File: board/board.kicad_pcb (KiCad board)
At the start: 4 copper layers, 45 x 157 mm, 47 parts, among them J1 020_1000BASE-T_with_CT, J2 020_1000BASE-T_with_CT, J3 020_1000BASE-T_with_CT, J4 020_1000BASE-T_with_CT, J5 020_1000BASE-T_with_CT, J6 011_GPIO, U1 RTL8367S-CG, Y1 25MhZ

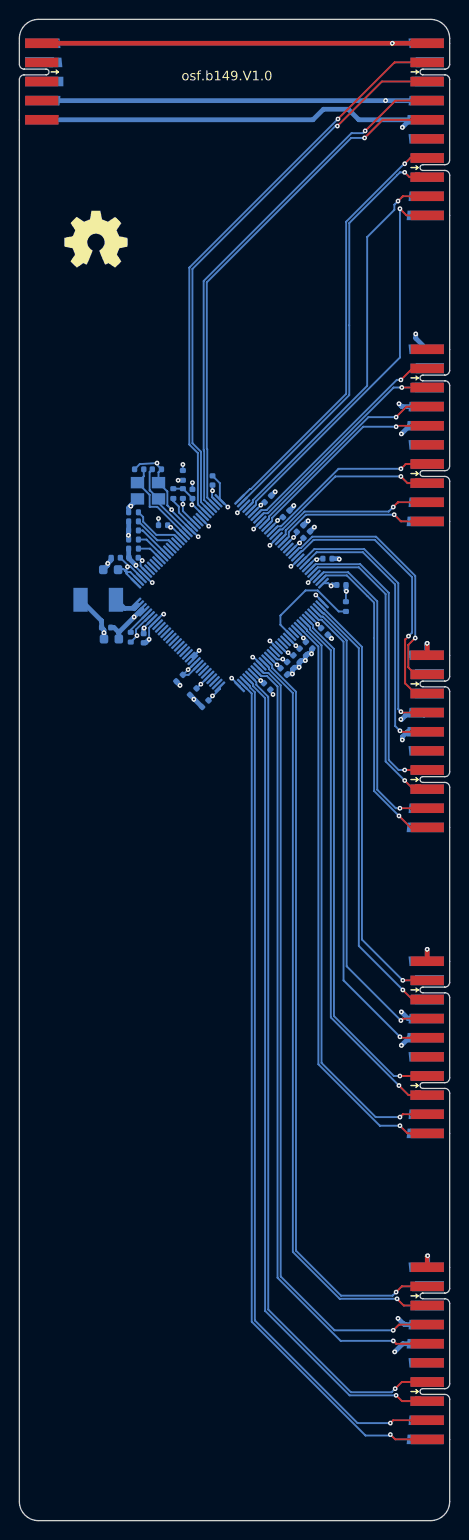
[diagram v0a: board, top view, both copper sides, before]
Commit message: added lcsc part numbers
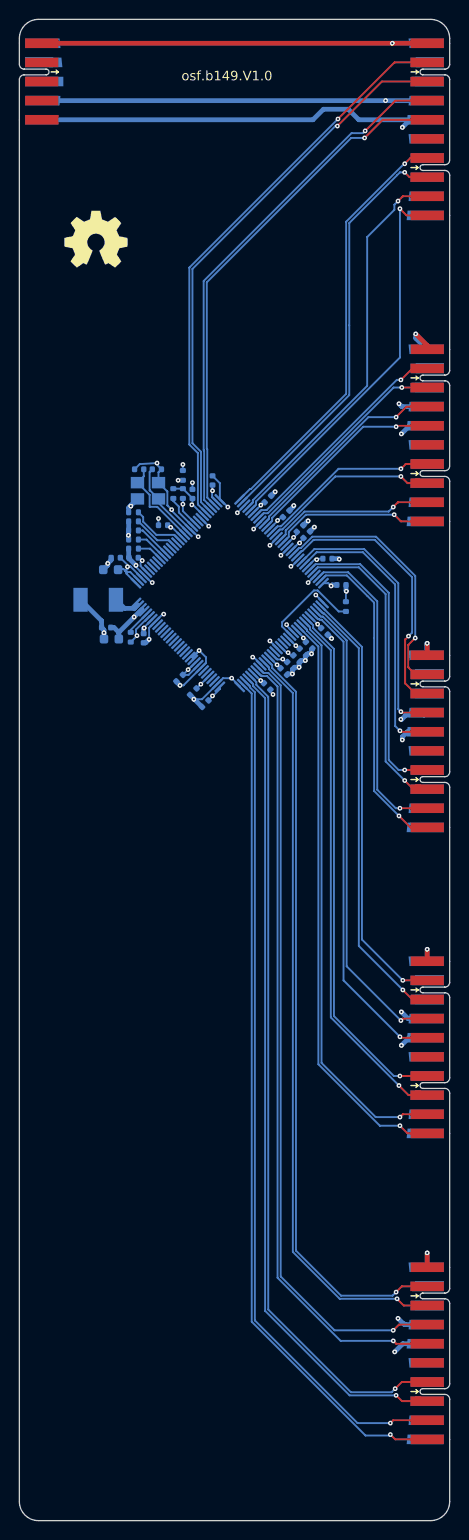
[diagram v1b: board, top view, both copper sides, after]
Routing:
- net GND: track 379.7 -> 396.6 mm, vias 44 -> 46
- net Net-(U1-MDIREF): track 11.4 -> 10.7 mm
